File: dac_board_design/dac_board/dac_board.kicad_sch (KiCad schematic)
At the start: 12 parts

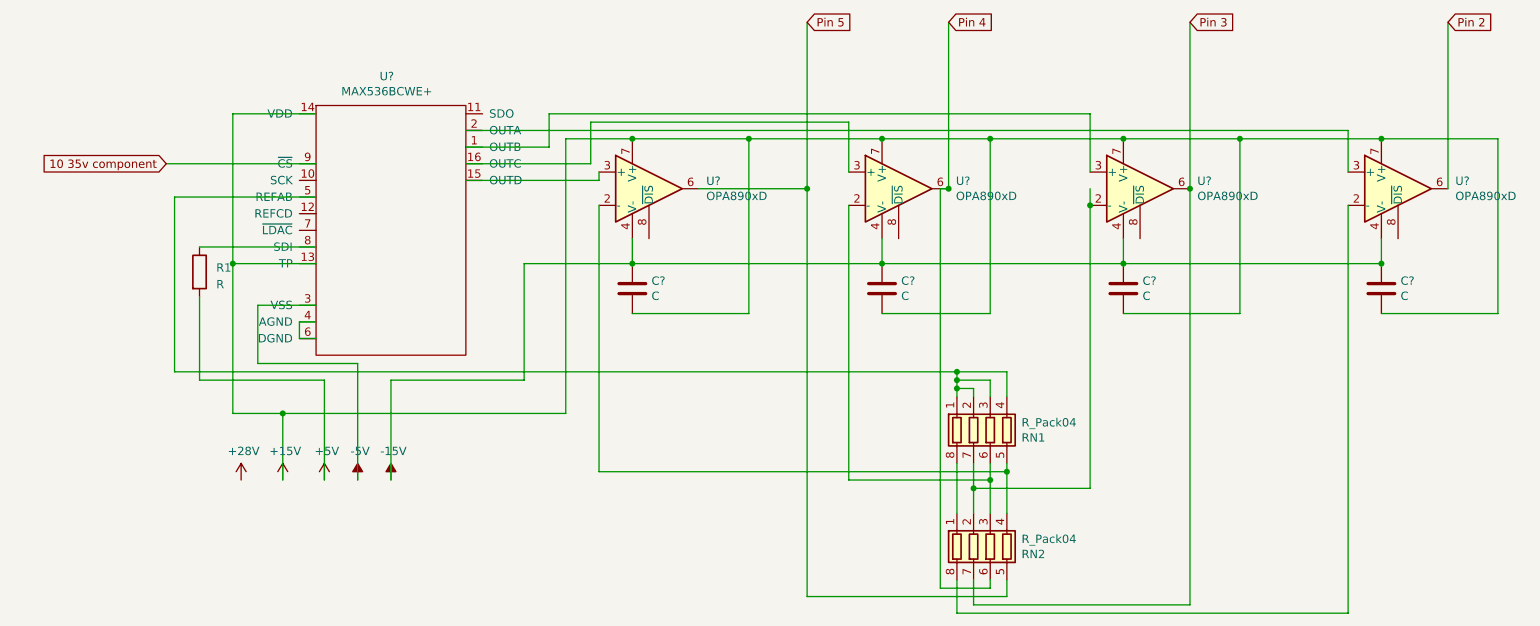
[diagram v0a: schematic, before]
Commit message: updating dac schematic
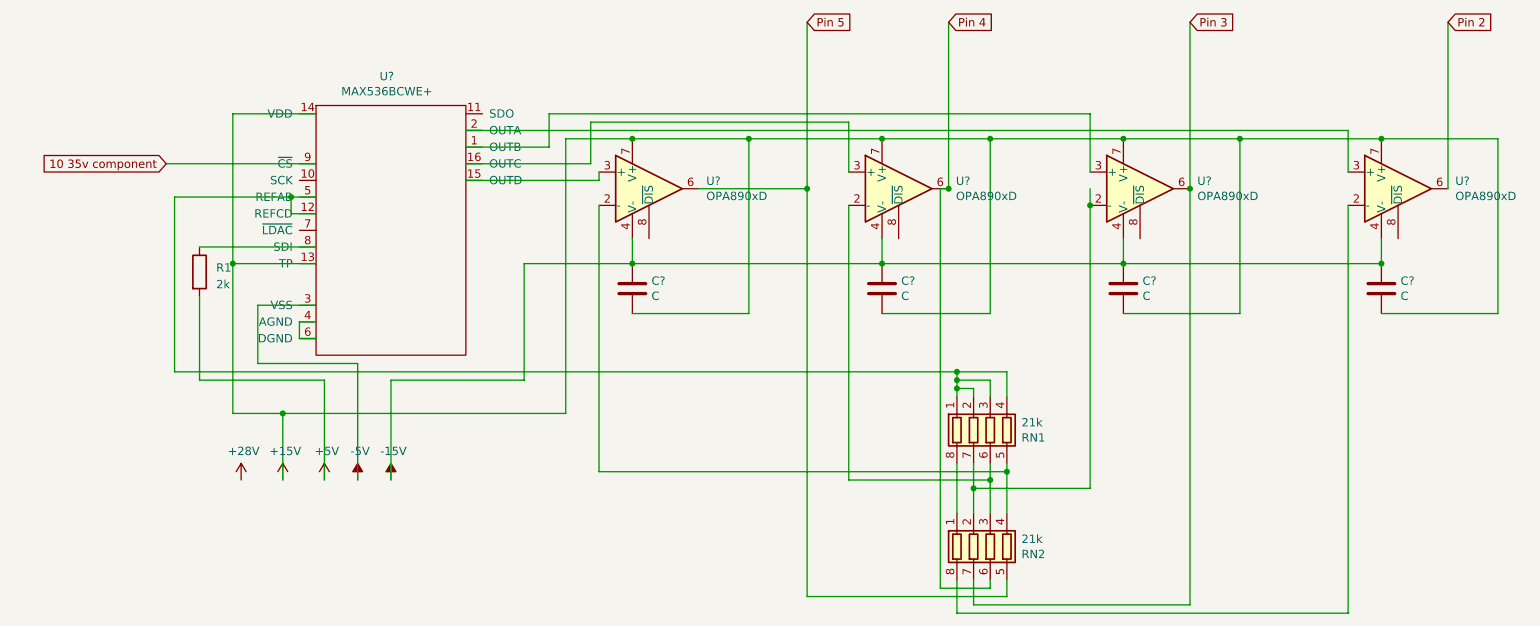
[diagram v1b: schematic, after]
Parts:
- R1: value R -> 2k
- RN1, RN2: value R_Pack04 -> 21k
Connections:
- net at U?.12 (REFCD): now also RN1.1 (R1.1), RN1.2 (R2.1), RN1.3 (R3.1), RN1.4 (R4.1), U?.5 (REFAB)
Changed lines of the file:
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@@
   (junction (at 133.35 41.91) (diameter 0) (color 0 0 0 0)
   )
+  (junction (at 33.02 43.18) (diameter 0) (color 0 0 0 0)
+  )
   (junction (at 85.09 53.34) (diameter 0) (color 0 0 0 0)
   )
@@
     (stroke (width 0) (type default))
   )
+  (wire (pts (xy 36.83 45.72) (xy 33.02 45.72))
+    (stroke (width 0) (type default))
+  )
   (wire (pts (xy 85.09 34.29) (xy 74.93 34.29))
     (stroke (width 0) (type default))
@@
     (stroke (width 0) (type default))
   )
+  (wire (pts (xy 33.02 43.18) (xy 15.24 43.18))
+    (stroke (width 0) (type default))
+  )
   (wire (pts (xy 38.1 86.36) (xy 38.1 71.12))
     (stroke (width 0) (type default))
@@
     (stroke (width 0) (type default))
   )
+  (wire (pts (xy 33.02 45.72) (xy 33.02 43.18))
+    (stroke (width 0) (type default))
+  )
   (wire (pts (xy 118.11 86.36) (xy 118.11 44.45))
     (stroke (width 0) (type default))
@@
     (stroke (width 0) (type default))
   )
-  (wire (pts (xy 36.83 43.18) (xy 15.24 43.18))
+  (wire (pts (xy 36.83 43.18) (xy 33.02 43.18))
     (stroke (width 0) (type default))
   )
@@
       (effects (font (size 1.27 1.27)) (justify left))
     )
-    (property "Value" "R_Pack04" (at 144.4752 95.377 0)
+    (property "Value" "21k" (at 144.4752 95.377 0)
       (effects (font (size 1.27 1.27)) (justify left))
     )
@@
       (effects (font (size 1.27 1.27)) (justify left))
     )
-    (property "Value" "R" (at 21.59 56.515 0)
+    (property "Value" "2k" (at 21.59 56.515 0)
       (effects (font (size 1.27 1.27)) (justify left))
     )
@@
       (effects (font (size 1.27 1.27)) (justify left))
     )
-    (property "Value" "R_Pack04" (at 144.4752 77.597 0)
-      (effects (font (size 1.27 1.27)) (justify left))
-    )
+    (property "Value" "21k" (at 144.4752 77.597 0)
+      (effects (font (size 1.27 1.27)) (justify left))
+    )
